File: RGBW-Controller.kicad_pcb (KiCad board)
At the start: 2 copper layers, 20 x 35 mm, 25 parts, among them J1 Conn_01x02, J2 Conn_01x05, Q1 AO3400A, Q2 AO3400A, Q3 AO3400A, Q4 AO3400A, U1 ESP-12F

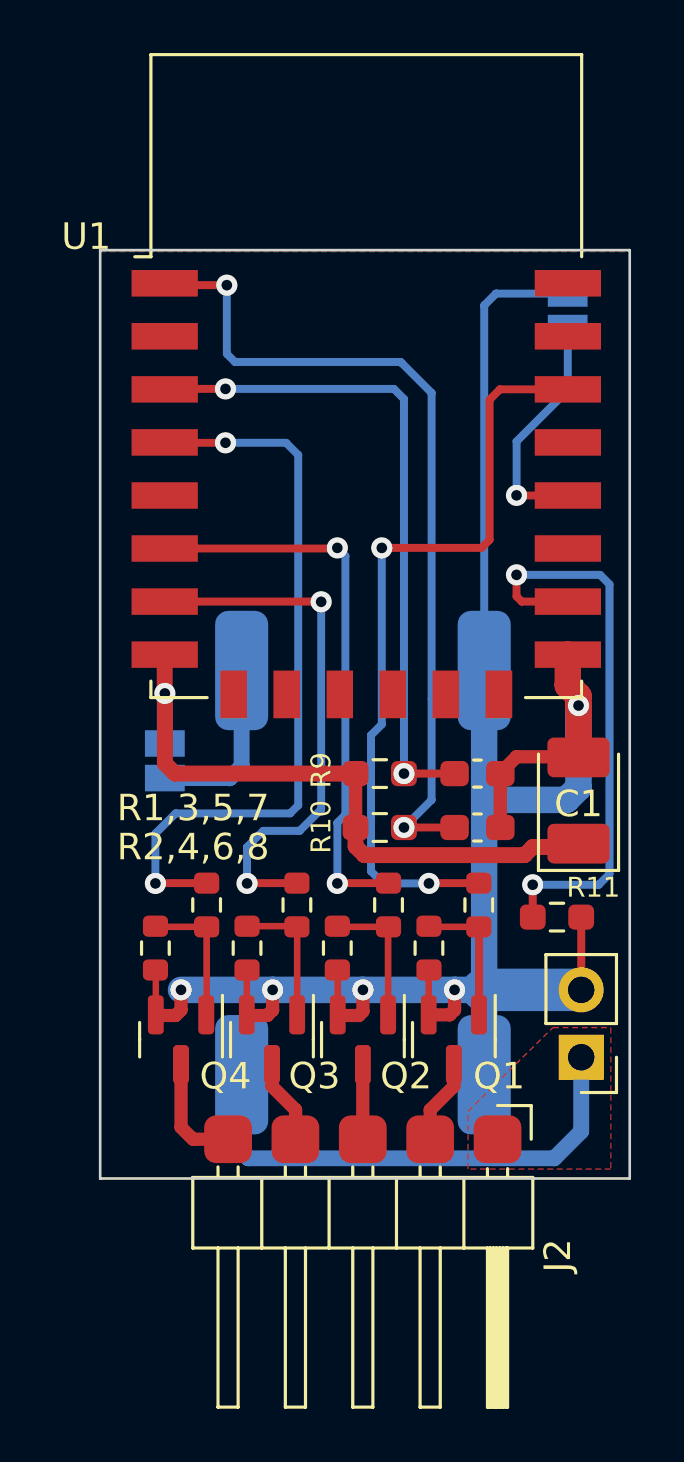
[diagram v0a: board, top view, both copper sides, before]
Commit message: updated footprint of C2 and C3
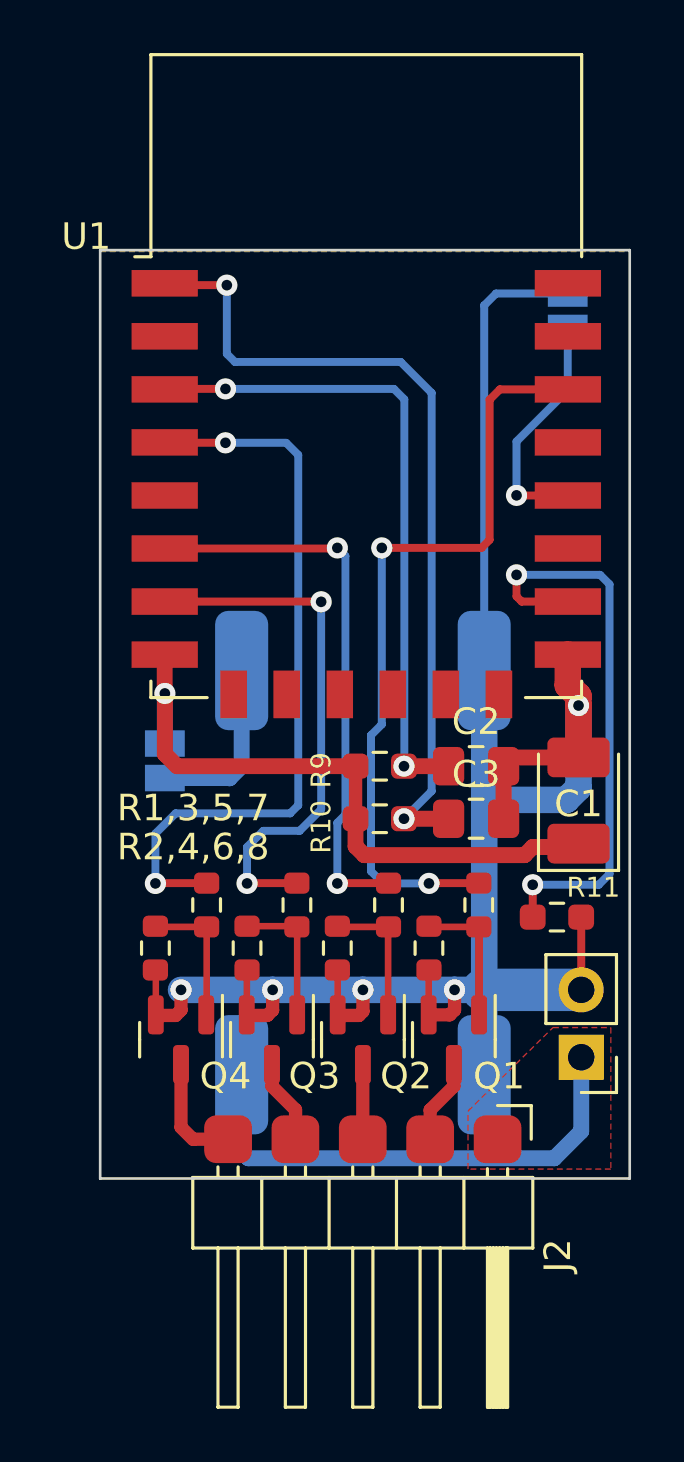
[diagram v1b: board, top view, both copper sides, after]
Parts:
- C2, C3: footprint Capacitor_SMD:C_0603_1608Metric_Pad1.08x0.95mm_HandSolder -> Capacitor_SMD:C_0805_2012Metric_Pad1.18x1.45mm_HandSolder
- J1: value Conn_01x02 -> Power
- J2: value Conn_01x05 -> RGBW
- JP1: renamed from Prog.; value Jumper_2_Open -> Prog
- JP2: renamed from 3V3; value Jumper_2_Open -> 3V3
- moved C3 0.33 mm to (140.7, 80.6)
- moved R10 0.33 mm to (137.0, 80.6)
- moved C2 0.28 mm to (140.7, 78.6)
- moved R9 0.28 mm to (137.0, 78.6)
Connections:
- JP2 pad 2: Net-(JP2-Pad2) -> Net-(A1-Pad3)

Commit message: Ground plane bug fixed
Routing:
- net +12V: track 19.0 -> 24.9 mm
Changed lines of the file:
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@@
     (fp_line (start 1 -0.625) (end 1 0.625) (layer "F.Fab") (width 0.1))
     (fp_line (start -1 -0.625) (end 1 -0.625) (layer "F.Fab") (width 0.1))
-    (pad "1" smd roundrect locked (at -1.0375 0) (size 1.175 1.45) (layers "F.Cu" "F.Paste" "F.Mask") (roundrect_rratio 0.212766)
+    (pad "1" smd roundrect locked (at -1.0375 0) (size 1.175 1.45) (layers "F.Cu" "F.Paste" "F.Mask") (roundrect_rratio 0.2127659574)
       (net 3 "EN") (pintype "passive"))
-    (pad "2" smd roundrect locked (at 1.0375 0) (size 1.175 1.45) (layers "F.Cu" "F.Paste" "F.Mask") (roundrect_rratio 0.212766)
+    (pad "2" smd roundrect locked (at 1.0375 0) (size 1.175 1.45) (layers "F.Cu" "F.Paste" "F.Mask") (roundrect_rratio 0.2127659574)
       (net 2 "GND") (pintype "passive"))
     (model "${KICAD6_3DMODEL_DIR}/Capacitor_SMD.3dshapes/C_0805_2012Metric.wrl"
@@
     (fp_line (start -1 0.625) (end -1 -0.625) (layer "F.Fab") (width 0.1))
     (fp_line (start -1 -0.625) (end 1 -0.625) (layer "F.Fab") (width 0.1))
-    (pad "1" smd roundrect locked (at -1.0375 0) (size 1.175 1.45) (layers "F.Cu" "F.Paste" "F.Mask") (roundrect_rratio 0.212766)
+    (pad "1" smd roundrect locked (at -1.0375 0) (size 1.175 1.45) (layers "F.Cu" "F.Paste" "F.Mask") (roundrect_rratio 0.2127659574)
       (net 4 "RST") (pintype "passive"))
-    (pad "2" smd roundrect locked (at 1.0375 0) (size 1.175 1.45) (layers "F.Cu" "F.Paste" "F.Mask") (roundrect_rratio 0.212766)
+    (pad "2" smd roundrect locked (at 1.0375 0) (size 1.175 1.45) (layers "F.Cu" "F.Paste" "F.Mask") (roundrect_rratio 0.2127659574)
       (net 2 "GND") (pintype "passive"))
     (model "${KICAD6_3DMODEL_DIR}/Capacitor_SMD.3dshapes/C_0805_2012Metric.wrl"
@@
   (segment (start 131.572 63.3476) (end 131.2672 63.0428) (width 0.3) (layer "B.Cu") (net 4))
   (segment (start 138.9888 64.516) (end 137.8204 63.3476) (width 0.3) (layer "B.Cu") (net 4))
+  (segment (start 144.6276 92.1004) (end 144.6276 89.5604) (width 1) (layer "F.Cu") (net 5))
+  (segment (start 141.473 92.653) (end 144.075 92.653) (width 1) (layer "F.Cu") (net 5))
+  (segment (start 144.075 92.653) (end 144.6276 92.1004) (width 1) (layer "F.Cu") (net 5))
   (segment (start 144.6276 92.3544) (end 143.6116 93.3704) (width 0.6) (layer "B.Cu") (net 5))
   (segment (start 132.08 93.3704) (end 131.826 93.1164) (width 0.6) (layer "B.Cu") (net 5))
@@
     )
   )
+  (zone (net 5) (net_name "+12V") (layer "F.Cu") (name "+12V") (hatch edge 0.508)
+    (priority 1)
+    (connect_pads yes (clearance 0.3))
+    (min_thickness 0.254) (filled_areas_thickness no)
+    (fill yes (thermal_gap 0.508) (thermal_bridge_width 0.508) (island_removal_mode 1) (island_area_min 0))
+    (polygon
+      (pts
+        (xy 146.4564 94.1324)
+        (xy 140.208 94.1324)
+        (xy 140.208 91.4908)
+        (xy 142.8496 88.392)
+        (xy 146.4564 88.392)
+      )
+    )
+  )
   (zone (net 0) (net_name "") (layer "F.Cu") (hatch edge 0.508)
     (connect_pads (clearance 0))
@@
       )
     )
-  )
-  (zone (net 5) (net_name "+12V") (layer "F.Cu") (hatch edge 0.508)
-    (connect_pads yes (clearance 0))
-    (min_thickness 0.254) (filled_areas_thickness no)
-    (fill yes (thermal_gap 0.508) (thermal_bridge_width 0.508))
-    (polygon
-      (pts
-        (xy 145.7452 93.7768)
-        (xy 140.3604 93.7768)
-        (xy 140.3604 91.5924)
-        (xy 143.5608 88.4428)
-        (xy 145.7452 88.4428)
-      )
-    )
